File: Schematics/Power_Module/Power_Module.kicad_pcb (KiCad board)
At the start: 4 copper layers, 69.5 x 60 mm, 110 parts, among them J1 ScrewSwitch A, J2 ScrewSwitch B, J3 Battery B, J4 USB_C_Female_USB2_Small, J5 Battery A, J6 Stack Male Edge Connector, Q1 AO4447A, Q2 AO4447A, U1 LMR51430XDDCR, U10 ISO1042BDWVR, U11 LM66100DCKR, U12 LM66100DCKR, U13 LM66100DCKR, U14 LM66100DCKR, U15 LM66100DCKR, U2 LMR51430XDDCR, U3 LMR51430XDDCR, U4 STM32F103C8Tx, U5 STM32F103C8Tx, U6 ACS37041KLHBLT-010B3, U7 ACS37041KLHBLT-010B3, U8 ACS37041KLHBLT-010B3, U9 AMS1117-3.3, Y1 X322516MMB4SI

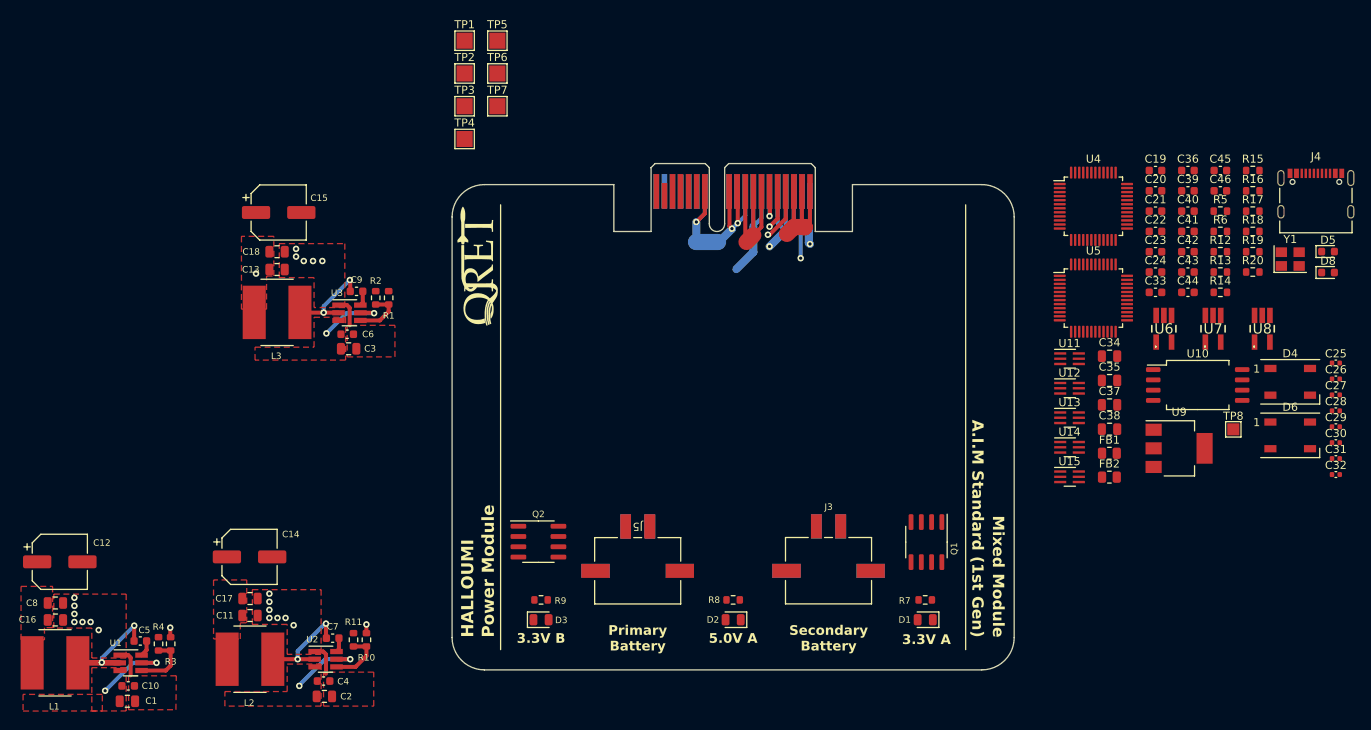
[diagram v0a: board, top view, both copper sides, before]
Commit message: Completed PCB layout
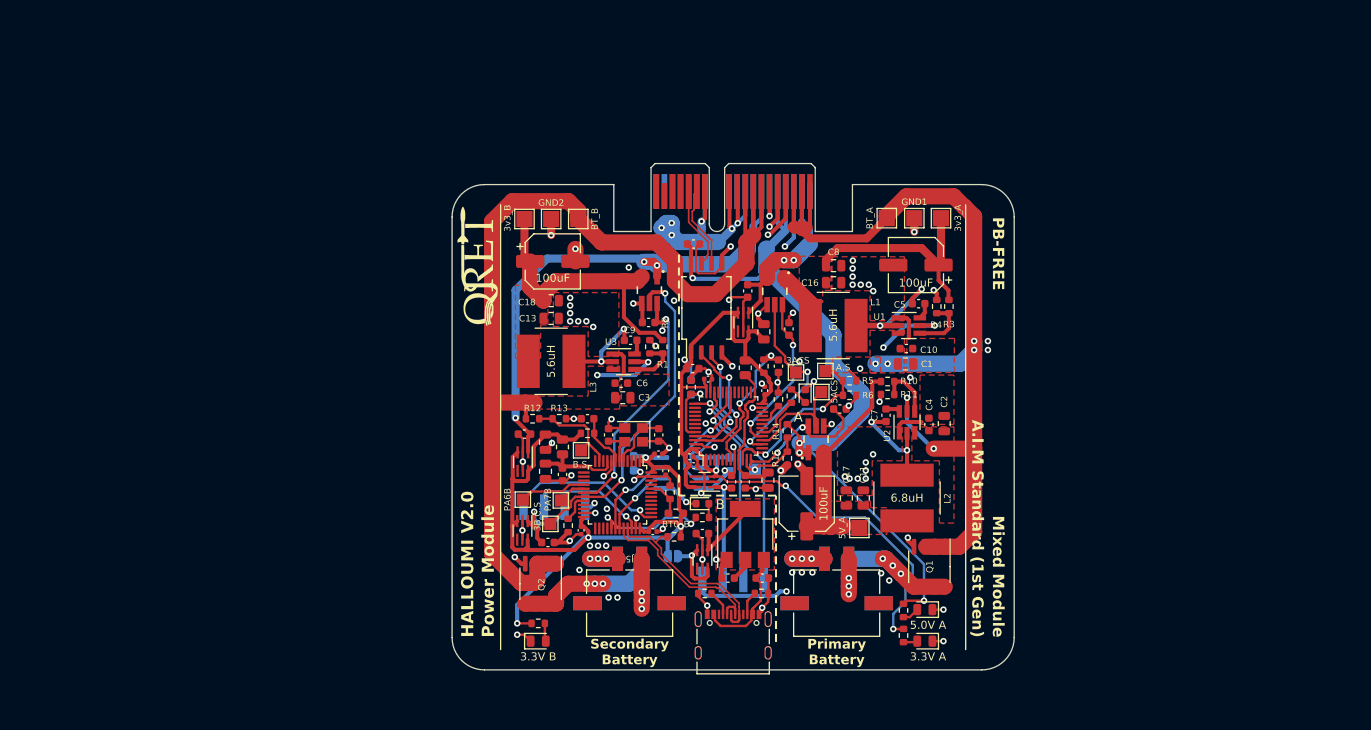
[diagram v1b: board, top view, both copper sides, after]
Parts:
- removed D4, D6: WS2812B, LED_SMD:LED_WS2812B_PLCC4_5.0x5.0mm_P3.2mm
- added C47: 100nF, Capacitor_SMD:C_0603_1608Metric, F.Cu at (147.0, 68.7)
- added C48: 100nF, Capacitor_SMD:C_0603_1608Metric, F.Cu at (170.6, 62.2)
- added C49: 0.1u, Capacitor_SMD:C_0603_1608Metric_Pad1.08x0.95mm_HandSolder, B.Cu at (164.6, 74.3)
- added C50: 0.1u, Capacitor_SMD:C_0603_1608Metric_Pad1.08x0.95mm_HandSolder, B.Cu at (152.7, 74.2)
- added J7: SWD_B, SWD_Header:SWD_PinHeader_1x04_P2.54mm_Horizontal_SMD, B.Cu at (146.7, 79.6)
- added J8: SWD_B, SWD_Header:SWD_PinHeader_1x04_P2.54mm_Horizontal_SMD, B.Cu at (161.2, 88.6)
- added JP1: USB_V_EN, Jumper:SolderJumper-2_P1.3mm_Open_RoundedPad1.0x1.5mm, B.Cu at (157.6, 85.7)
- added R21: 10k, Resistor_SMD:R_0603_1608Metric, F.Cu at (147.0, 70.5)
- added R22: 10k, Resistor_SMD:R_0603_1608Metric, F.Cu at (168.8, 62.2)
- added R23: 100k, Resistor_SMD:R_0603_1608Metric, F.Cu at (159.8, 64.8)
- added R24: BT0_A, Resistor_SMD:R_0603_1608Metric_Pad0.98x0.95mm_HandSolder, B.Cu at (159.8, 64.8)
- added R25: 100k, Resistor_SMD:R_0603_1608Metric, F.Cu at (170.6, 66.3)
- added R26: 100k, Resistor_SMD:R_0603_1608Metric, F.Cu at (157.2, 77.8)
- added R27: BT0_B, Resistor_SMD:R_0603_1608Metric_Pad0.98x0.95mm_HandSolder, F.Cu at (157.9, 80.4)
- added R28: 100k, Resistor_SMD:R_0603_1608Metric, F.Cu at (144.6, 81.9)
- added TP10: B.S, TestPoint:TestPoint_Pad_1.5x1.5mm, F.Cu at (146.2, 72.6)
- added TP11: 3B.C.S, TestPoint:TestPoint_Pad_1.5x1.5mm, F.Cu at (142.4, 81.7)
- added TP12: 3ACS, TestPoint:TestPoint_Pad_1.5x1.5mm, F.Cu at (172.8, 63.0)
- added TP13: 5ACS, TestPoint:TestPoint_Pad_1.5x1.5mm, F.Cu at (175.9, 65.4)
- added TP16: PA7B, TestPoint:TestPoint_Pad_1.5x1.5mm, F.Cu at (143.7, 78.8)
- added TP17: PA6B, TestPoint:TestPoint_Pad_1.5x1.5mm, F.Cu at (139.0, 78.7)
- added TP9: A.S, TestPoint:TestPoint_Pad_1.5x1.5mm, F.Cu at (176.4, 62.8)
- added U16: SCM3721ASA, Package_SO:SOIC-8_3.9x4.9mm_P1.27mm, B.Cu at (158.6, 75.4)
- J1: value ScrewSwitch A -> ScrewSwitch B
- J2: value ScrewSwitch B -> ScrewSwitch A
- J3: value Battery B -> Battery A
- J5: value Battery A -> Battery B
- R9: value 1.2k -> 3.3k
- TP1: value TP_BATT1 -> BT_A
- TP2: value TP_BATT2 -> BT_B
- TP3: value TP_GND2 -> GND2
- TP4: value TP_GND1 -> GND1
- TP5: value TP_3.3V_A -> 3v3_A
- TP6: value TP_5.0V_A -> 5V_A
- TP7: value TP_3.3V_B -> 3v3_B
- TP8: value TP_GND -> 5VSENS; moved to B.Cu
- moved C12 112.0 mm to (187.6, 49.7), turned to 180 degrees
- moved R3 104.9 mm to (191.7, 54.8)
- moved C1 104.9 mm to (186.3, 61.9)
- moved C8 104.9 mm to (177.4, 49.8)
- moved C16 104.9 mm to (177.4, 51.9)
- moved U1 104.9 mm to (186.7, 57.2)
- moved C10 104.9 mm to (186.4, 60.0)
- moved C5 104.9 mm to (187.9, 54.5)
- moved R4 104.9 mm to (190.2, 54.8)
- moved L1 104.9 mm to (177.4, 57.2)
- moved C31 93.7 mm to (146.2, 82.5), turned to 90 degrees
- moved J4 90.4 mm to (165.0, 95.4)
- moved C41 88.0 mm to (142.1, 84.0)
- moved R12 87.5 mm to (140.2, 68.7)
- moved C39 87.4 mm to (139.2, 70.6), turned to 180 degrees
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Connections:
- net CAN_H renamed CAN_+
- net CAN_L renamed CAN_-
- C44 pad 1: V_MUX_A -> 3.3V_A_ACS_PWR
- C45 pad 1: V_MUX_A -> 5.0V_A_ACS_PWR
- C46 pad 1: V_MUX_B -> 3.3V_B_ACS_PWR
- J3 pad 1: GND2 -> GND
- J5 pad 1: GND -> GND2
- Q1 pad 5: Net-(J1-Pad2) -> Net-(J2-Pad2)
- Q1 pad 6: Net-(J1-Pad2) -> Net-(J2-Pad2)
- Q1 pad 7: Net-(J1-Pad2) -> Net-(J2-Pad2)
- Q1 pad 8: Net-(J1-Pad2) -> Net-(J2-Pad2)
- Q2 pad 5: Net-(J2-Pad2) -> Net-(J1-Pad2)
- Q2 pad 6: Net-(J2-Pad2) -> Net-(J1-Pad2)
- Q2 pad 7: Net-(J2-Pad2) -> Net-(J1-Pad2)
- Q2 pad 8: Net-(J2-Pad2) -> Net-(J1-Pad2)
- R12 pad 1: unconnected-(R12-Pad1) -> BATT_B
- R12 pad 2: unconnected-(R12-Pad2) -> BATT_B_SENSE
- R13 pad 1: unconnected-(R13-Pad1) -> BATT_B_SENSE
- R13 pad 2: unconnected-(R13-Pad2) -> GND2
- R14 pad 1: unconnected-(R14-Pad1) -> 5.0V_A
- R14 pad 2: unconnected-(R14-Pad2) -> 5.0V_A_SENSE
- R15 pad 1: unconnected-(R15-Pad1) -> 5.0V_A_SENSE
- R15 pad 2: unconnected-(R15-Pad2) -> GND
- R5 pad 1: unconnected-(R5-Pad1) -> BATT_A
- R5 pad 2: unconnected-(R5-Pad2) -> BATT_A_SENSE
- R6 pad 1: unconnected-(R6-Pad1) -> BATT_A_SENSE
- R6 pad 2: unconnected-(R6-Pad2) -> GND
- R7 pad 1: 3.3V_A -> V_MUX_A
- R9 pad 1: 3.3V_B -> V_MUX_B
- TP8 pad 1: unconnected-(TP8-Pad1) -> 5.0V_A_SENSE
- U12 pad 3: V_MUX_B -> Net-(JP1-B)
- U12 pad 6: V_MUX_B -> Net-(JP1-B)
- U4 pad 1: Net-(U4-VBAT) -> V_MUX_A
- U4 pad 10: unconnected-(U4-PA0-Pad10) -> BATT_A_SENSE
- U4 pad 11: unconnected-(U4-PA1-Pad11) -> 5.0V_A_SENSE
- U4 pad 12: unconnected-(U4-PA2-Pad12) -> 5.0V_A_ACS_PWR
- U4 pad 14: unconnected-(U4-PA4-Pad14) -> 3.3V_A_CURR_SENSE
- U4 pad 15: unconnected-(U4-PA5-Pad15) -> 5.0V_A_CURR_SENSE
- U4 pad 16: unconnected-(U4-PA6-Pad16) -> 3.3V_A_ACS_PWR
- U4 pad 17: unconnected-(U4-PA7-Pad17) -> DB_LED_A
- U4 pad 24: Net-(U4-VBAT) -> V_MUX_A
- U4 pad 30: unconnected-(U4-PA9-Pad30) -> TX_A
- U4 pad 31: unconnected-(U4-PA10-Pad31) -> RX_A
- U4 pad 36: Net-(U4-VBAT) -> V_MUX_A
- U4 pad 38: DB_LED_A -> unconnected-(U4-PA15-Pad38)
- U4 pad 39: RGB_DATA -> unconnected-(U4-PB3-Pad39)
- U4 pad 48: Net-(U4-VBAT) -> V_MUX_A
- U4 pad 9: unconnected-(U4-VDDA-Pad9) -> 3.3VA_A
- U5 pad 1: unconnected-(U5-VBAT-Pad1) -> V_MUX_B
- U5 pad 11: unconnected-(U5-PA1-Pad11) -> BATT_B_SENSE
- U5 pad 16: unconnected-(U5-PA6-Pad16) -> Net-(U5-PA6)
- U5 pad 17: unconnected-(U5-PA7-Pad17) -> Net-(U5-PA7)
- U5 pad 18: unconnected-(U5-PB0-Pad18) -> 3.3V_B_ACS_PWR
- U5 pad 19: unconnected-(U5-PB1-Pad19) -> 3.3V_B_CURR_SENSE
- U5 pad 24: unconnected-(U5-VDD-Pad24) -> V_MUX_B
- U5 pad 29: unconnected-(U5-PA8-Pad29) -> DB_LED_B
- U5 pad 30: unconnected-(U5-PA9-Pad30) -> TX_B
- U5 pad 31: unconnected-(U5-PA10-Pad31) -> RX_B
- U5 pad 36: unconnected-(U5-VDD-Pad36) -> V_MUX_B
- U5 pad 38: DB_LED_B -> unconnected-(U5-PA15-Pad38)
- U5 pad 48: unconnected-(U5-VDD-Pad48) -> V_MUX_B
- U5 pad 9: unconnected-(U5-VDDA-Pad9) -> 3.3VA_B
- U6 pad 4: unconnected-(U6-VOUT-Pad4) -> 3.3V_A_CURR_SENSE
- U6 pad 5: V_MUX_A -> 3.3V_A_ACS_PWR
- U7 pad 1: 5.0V_A_Pre -> 5.0V_A
- U7 pad 2: 5.0V_A -> 5.0V_A_Pre
- U7 pad 4: unconnected-(U7-VOUT-Pad4) -> 5.0V_A_CURR_SENSE
- U7 pad 5: V_MUX_A -> 5.0V_A_ACS_PWR
- U8 pad 1: 3.3V_B_Pre -> 3.3V_B
- U8 pad 2: 3.3V_B -> 3.3V_B_Pre
- U8 pad 4: unconnected-(U8-VOUT-Pad4) -> 3.3V_B_CURR_SENSE
- U8 pad 5: V_MUX_B -> 3.3V_B_ACS_PWR
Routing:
- net V_MUX_A: track 0.00 -> 106.3 mm, vias 0 -> 4
- net BATT_B: track 27.5 -> 130.2 mm
- net V_MUX_B: track 0.00 -> 97.9 mm, vias 0 -> 4
- net BATT_A: track 35.1 -> 125.8 mm, vias 4 -> 8
- net GND: track 33.7 -> 122.0 mm, vias 18 -> 58
- net GND2: track 33.8 -> 121.7 mm, vias 8 -> 52
- net 5.0V_A: track 12.9 -> 97.4 mm, vias 1 -> 4
- net 3.3V_B: track 14.8 -> 68.0 mm, vias 1 -> 3
- net 3.3V_B_CURR_SENSE: track 0.00 -> 40.9 mm, vias 0 -> 2
- net 3.3V_B_Pre: track 0.00 -> 35.4 mm
- net 3.3V_A_Pre: track 1.20 -> 34.1 mm, vias 1 -> 0
- net 3.3V_B_ACS_PWR: track 0.00 -> 30.9 mm, vias 0 -> 2
- net SWCLK_A: track 0.00 -> 26.7 mm, vias 0 -> 1
- net SWDIO_A: track 0.00 -> 25.7 mm, vias 0 -> 1
- net 5.0V_A_Pre: track 1.08 -> 26.3 mm, vias 1 -> 0
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- added copper zone on F.Cu, net 3.3V_A_Pre
- added copper zone on F.Cu, net 3.3V_B_Pre
- added copper zone on F.Cu, net 5.0V_A_Pre
- added copper zone on In1.Cu, net GND2
- added copper zone on In2.Cu, net GND2
- added copper zone on F.Cu, net V_REGUSB_B
- removed copper zone on F.Cu, net 3.3V_A
- removed copper zone on F.Cu, net 3.3V_B
- removed copper zone on F.Cu, net 5.0V_A
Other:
- board text added: "A"
- board text added: "B"
- board text added: "HALLOUMI V2.0"
- board text added: "Halloumi Rev 2.0 QRET Feb 2025 Rajan Laird Kennan Bays Oak Campbell"
- board text added: "Most annoying PCB we've made to date"
- board text added: "PB-FREE"
- board text removed: "HALLOUMI"
- board text removed: "locked"

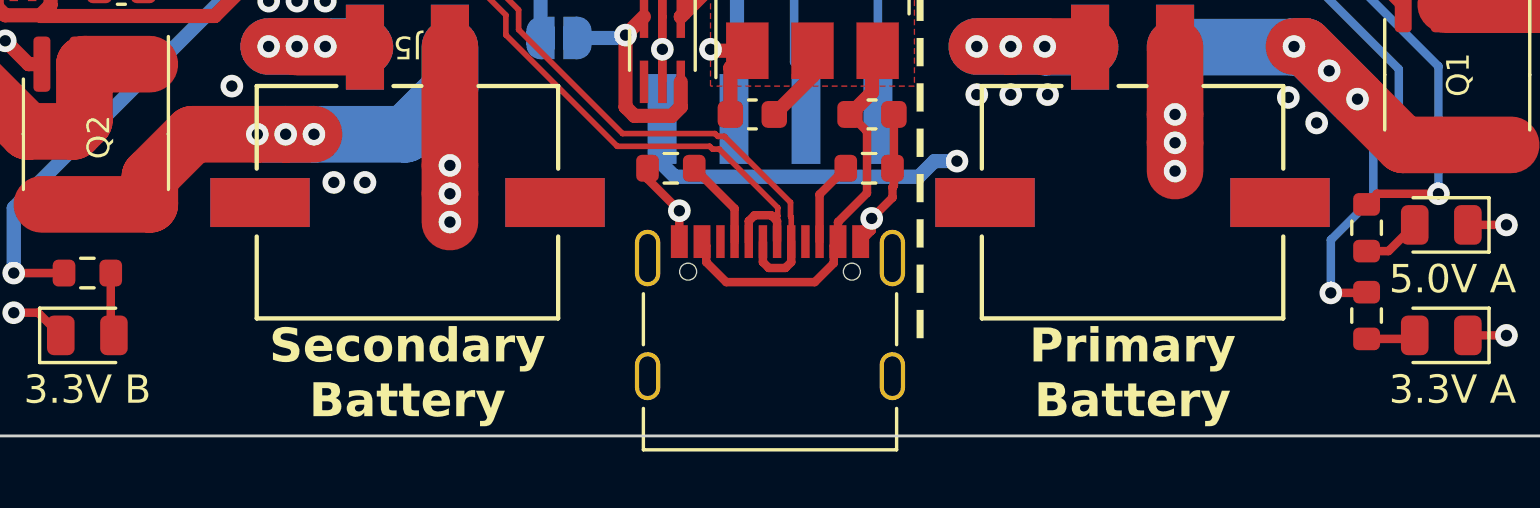
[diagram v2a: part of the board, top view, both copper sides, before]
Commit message: Tweaked silkscreen
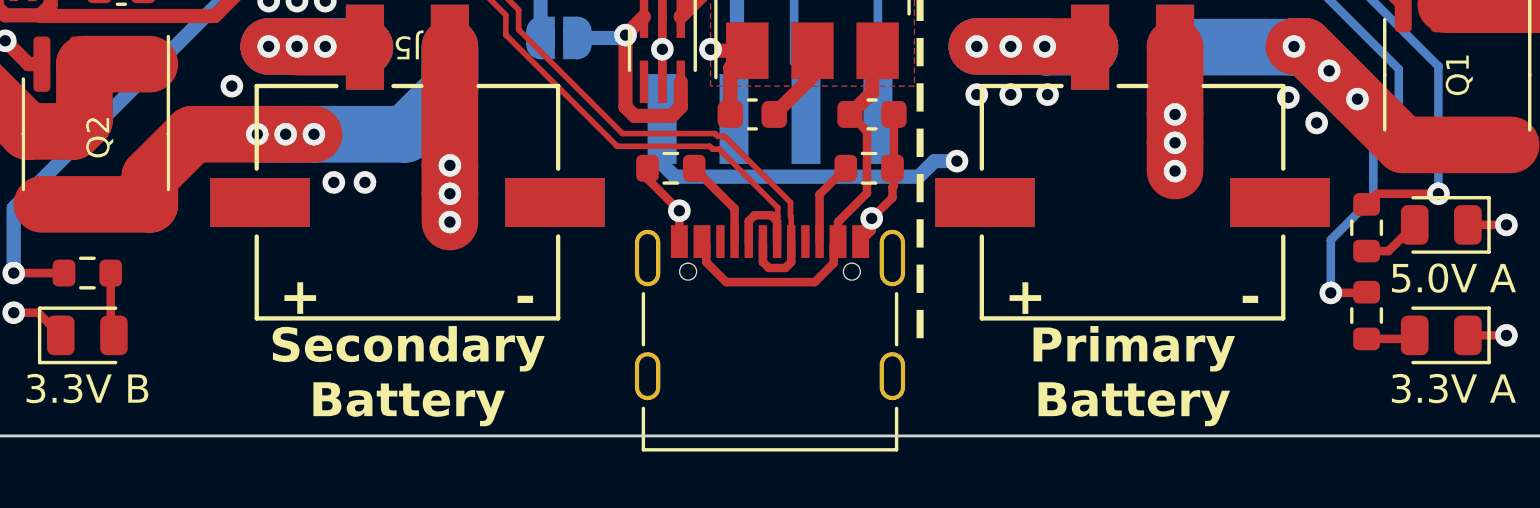
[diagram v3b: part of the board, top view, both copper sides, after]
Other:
- board text added: "+ -"
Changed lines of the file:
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@@
     (effects (font (size 1.4 1.4) (thickness 0.25) bold) (justify left bottom mirror))
+  )
+  (gr_text "A" (at 167.5 98.9) (layer "B.SilkS")
+    (effects (font (size 1.2 1.2) (thickness 0.2) bold) (justify bottom mirror))
   )
   (gr_text "Primary\nSwitch" (at 177.8 99.2) (layer "B.SilkS")
     (effects (font (size 1.2 1.2) (thickness 0.2) bold) (justify bottom mirror))
   )
+  (gr_text "B" (at 140.4 69.2 180) (layer "B.SilkS")
+    (effects (font (size 1.2 1.2) (thickness 0.2) bold) (justify bottom mirror))
+  )
   (gr_text "3.3V B" (at 140.9 98.7) (layer "F.SilkS" knockout)
     (effects (font (size 1 1) (thickness 0.15)) (justify bottom))
+  )
+  (gr_text "+           -" (at 177.8 95.6007) (layer "F.SilkS")
+    (effects (font (size 1.3 1.3) (thickness 0.25) bold) (justify bottom))
   )
   (gr_text "Mixed Module" (at 196.95 95.749998 -90) (layer "F.SilkS")
@@
     (effects (font (size 1 1) (thickness 0.15)) (justify bottom))
   )
+  (gr_text "+           -" (at 152.2 95.6007) (layer "F.SilkS")
+    (effects (font (size 1.3 1.3) (thickness 0.25) bold) (justify bottom))
+  )
   (gr_text "B" (at 163.4 80) (layer "F.SilkS" knockout)

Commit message: Added/fixed part numbers
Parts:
- R14: value 60k -> 30k
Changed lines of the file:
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@@
     (descr "LH,5-Pin  SOT23-W")
     (tags "Integrated Circuit")
+    (property "Digikey" "620-ACS37041KLHBLT-010B3CT-ND")
     (property "Height" "1.13")
     (property "Sheetfile" "Power_Module.kicad_sch")
@@
     (descr "LQFP, 48 Pin (https://www.analog.com/media/en/technical-documentation/data-sheets/ltc2358-16.pdf), generated with kicad-footprint-generator ipc_gullwing_generator.py")
     (tags "LQFP QFP")
+    (property "JLCPCB" "C8304")
     (property "Sheetfile" "Power_Module.kicad_sch")
     (property "Sheetname" "")
@@
     (descr "Resistor SMD 0603 (1608 Metric), square (rectangular) end terminal, IPC_7351 nominal, (Body size source: IPC-SM-782 page 72, https://www.pcb-3d.com/wordpress/wp-content/uploads/ipc-sm-782a_amendment_1_and_2.pdf), generated with kicad-footprint-generator")
     (tags "resistor")
-    (property "JLCPCB" "")
+    (property "JLCPCB" "C25804")
     (property "Sheetfile" "Power_Module.kicad_sch")
     (property "Sheetname" "")
@@
         (effects (font (size 0.8 0.8) (thickness 0.1)))
     )
-    (fp_text value "60k" (at 0 1.43 90) (layer "F.Fab")
+    (fp_text value "30k" (at 0 1.43 90) (layer "F.Fab")
         (effects (font (size 1 1) (thickness 0.15)))
     )
@@
     (descr "LH,5-Pin  SOT23-W")
     (tags "Integrated Circuit")
+    (property "Digikey" "620-ACS37041KLHBLT-010B3CT-ND")
     (property "Height" "1.13")
     (property "Sheetfile" "Power_Module.kicad_sch")
@@
     (descr "LQFP, 48 Pin (https://www.analog.com/media/en/technical-documentation/data-sheets/ltc2358-16.pdf), generated with kicad-footprint-generator ipc_gullwing_generator.py")
     (tags "LQFP QFP")
+    (property "JLCPCB" "C8304")
     (property "Sheetfile" "Power_Module.kicad_sch")
     (property "Sheetname" "")
@@
     (descr "LH,5-Pin  SOT23-W")
     (tags "Integrated Circuit")
+    (property "Digikey" "620-ACS37041KLHBLT-010B3CT-ND")
     (property "Height" "1.13")
     (property "Sheetfile" "Power_Module.kicad_sch")
@@
     (descr "SOIC, 8 Pin (JEDEC MS-012AA, https://www.analog.com/media/en/package-pcb-resources/package/pkg_pdf/soic_narrow-r/r_8.pdf), generated with kicad-footprint-generator ipc_gullwing_generator.py")
     (tags "SOIC SO")
+    (property "Digikey" "2725-SCM3721ASACT-ND")
     (property "Sheetfile" "Power_Module.kicad_sch")
     (property "Sheetname" "")

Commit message: Tweaked some part numbers
-Changed STM32F103CB to STM32F103C8
-Changed USB port to C5178541
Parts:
- U4, U5: value STM32F103C8Tx -> STM32F103C8T6
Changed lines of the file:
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@@
     (descr "LQFP, 48 Pin (https://www.analog.com/media/en/technical-documentation/data-sheets/ltc2358-16.pdf), generated with kicad-footprint-generator ipc_gullwing_generator.py")
     (tags "LQFP QFP")
-    (property "JLCPCB" "C8304")
+    (property "JLCPCB" "C8734")
     (property "Sheetfile" "Power_Module.kicad_sch")
     (property "Sheetname" "")
@@
         (effects (font (size 0.8 0.8) (thickness 0.1)))
     )
-    (fp_text value "STM32F103C8Tx" (at 0 5.85 90) (layer "F.Fab")
+    (fp_text value "STM32F103C8T6" (at 0 5.85 90) (layer "F.Fab")
         (effects (font (size 1 1) (thickness 0.15)))
     )
@@
     (descr "Resistor SMD 0603 (1608 Metric), square (rectangular) end terminal, IPC_7351 nominal, (Body size source: IPC-SM-782 page 72, https://www.pcb-3d.com/wordpress/wp-content/uploads/ipc-sm-782a_amendment_1_and_2.pdf), generated with kicad-footprint-generator")
     (tags "resistor")
-    (property "JLCPCB" "C25804")
+    (property "JLCPCB" "C22984")
     (property "Sheetfile" "Power_Module.kicad_sch")
     (property "Sheetname" "")
@@
     (descr "Resistor SMD 0603 (1608 Metric), square (rectangular) end terminal, IPC_7351 nominal, (Body size source: IPC-SM-782 page 72, https://www.pcb-3d.com/wordpress/wp-content/uploads/ipc-sm-782a_amendment_1_and_2.pdf), generated with kicad-footprint-generator")
     (tags "resistor")
-    (property "JLCPCB" "C25804")
+    (property "JLCPCB" "C22984")
     (property "Sheetfile" "Power_Module.kicad_sch")
     (property "Sheetname" "")
@@
     (descr "LQFP, 48 Pin (https://www.analog.com/media/en/technical-documentation/data-sheets/ltc2358-16.pdf), generated with kicad-footprint-generator ipc_gullwing_generator.py")
     (tags "LQFP QFP")
-    (property "JLCPCB" "C8304")
+    (property "JLCPCB" "C8734")
     (property "Sheetfile" "Power_Module.kicad_sch")
     (property "Sheetname" "")
@@
         (effects (font (size 0.8 0.8) (thickness 0.1)))
     )
-    (fp_text value "STM32F103C8Tx" (at -1.42 7.2875 90) (layer "F.Fab")
+    (fp_text value "STM32F103C8T6" (at -1.42 7.2875 90) (layer "F.Fab")
         (effects (font (size 1 1) (thickness 0.15)))
     )
@@
     (descr "https://wmsc.lcsc.com/wmsc/upload/file/pdf/v2/lcsc/2201121730_HDGC-TYPE-C-DB-108PWB_C2936184.pdf")
     (tags "USB C Type-C Receptacle Female USB2.0")
-    (property "JLCPCB" "C2936184")
+    (property "JLCPCB" "C5178541")
     (property "Sheetfile" "Power_Module.kicad_sch")
     (property "Sheetname" "")

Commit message: Added polarity markings to switch connectors
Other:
- board text added: "- +"
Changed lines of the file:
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@@
     )
+  )
+  (gr_text "-           +" (at 152.2 95.6007) (layer "B.SilkS")
+    (effects (font (size 1.3 1.3) (thickness 0.25) bold) (justify bottom mirror))
+  )
+  (gr_text "-           +" (at 177.8 95.6007) (layer "B.SilkS")
+    (effects (font (size 1.3 1.3) (thickness 0.25) bold) (justify bottom mirror))
   )
   (gr_text "Halloumi Rev 2.0\nQRET Feb 2025\n\nRajan Laird\nKennan Bays\nOak Campbell" (at 165 46.7) (layer "B.SilkS")
